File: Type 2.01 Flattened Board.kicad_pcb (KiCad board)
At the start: 4 copper layers, 170 x 170 mm, 68 parts, among them J1 Conn_02x03_Odd_Even, J4 Conn_02x03_Odd_Even, J5 Conn_02x03_Odd_Even, U1 74AHC74, U10 74AHC74, U11 74AHC245, U13 74AHC04, U14 ATmega4809-PF, U16 ATmega4809-PF, U17 74AHC157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

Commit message: Part selection
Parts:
- removed RN2, RN3: R_Network04, Resistor_THT:R_Array_SIP5
- added J2: Conn_01x02, Connector_PinHeader_2.54mm:PinHeader_1x02_P2.54mm_Vertical, F.Cu at (179.7, 107.8)
- added J3: Conn_01x04, Connector_PinHeader_2.54mm:PinHeader_1x04_P2.54mm_Vertical, F.Cu at (175.0, 107.8)
- moved C20 84.1 mm to (108.7, 121.7), turned to -90 degrees
- moved U13 76.4 mm to (114.4, 123.6), turned to 90 degrees
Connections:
- RN1 pad 10: unconnected-(RN1-Pad10) -> /i960/PU2
- RN1 pad 11: unconnected-(RN1-Pad11) -> /i960/PU3
- RN1 pad 12: unconnected-(RN1-Pad12) -> /i960/~{MR_{0}}
- RN1 pad 8: unconnected-(RN1-Pad8) -> /i960/PU0
- RN1 pad 9: unconnected-(RN1-Pad9) -> /i960/PU1
- U13 pad 6: /i960/~{INT3}_OUT -> /i960/i960.~{INT0}
- U13 pad 8: /i960/~{INT0}_OUT -> /i960/i960.~{INT3}
- U14 pad 36: Net-(U13-Pad5) -> /i960/INT3_OUT
- U14 pad 4: Net-(U13-Pad9) -> /i960/INT0_OUT
- U16 pad 10: /i960/EDGE_A -> /i960/EDGE_B
- U16 pad 11: /i960/EDGE_B -> /i960/~{ME_READY}
- U16 pad 9: /i960/~{ME_READY} -> /i960/EDGE_A
- U17 pad 12: /i960/i960.~{INT3} -> Net-(U13-Pad9)
- U17 pad 13: +5V -> GND
- U17 pad 14: /i960/~{INT3}_OUT -> /i960/INT3_OUT
- U17 pad 2: /i960/~{INT0}_OUT -> /i960/INT0_OUT
- U17 pad 3: +5V -> GND
- U17 pad 4: /i960/i960.~{INT0} -> Net-(U13-Pad5)

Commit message: Added feather interrupts as well
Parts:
- removed J1: Conn_02x03_Odd_Even, Connector_IDC:IDC-Header_2x03_P2.54mm_Horizontal
- C20, C5, U13, U17: moved to B.Cu
- U10: value 74AHC74 -> 74AHC174; footprint Package_DIP:DIP-14_W7.62mm_Socket -> Package_SO:SOIC-16_3.9x9.9mm_P1.27mm
- moved J5 171.9 mm to (14.0, 82.2), turned to 180 degrees
- moved J4 119.1 mm to (13.9, 100.7), turned to 180 degrees
- moved C19 106.9 mm to (27.5, 72.8), turned to -90 degrees
- moved U4 99.5 mm to (35.3, 76.9), turned to 90 degrees
- moved U14 86.8 mm to (125.1, 145.0), turned to 90 degrees
- moved U20 85.4 mm to (-78.0, 106.7)
- moved C26 70.3 mm to (136.5, 147.7), turned to 0 degrees
- moved C25 69.7 mm to (146.7, 127.1), turned to 180 degrees
- moved C4 59.0 mm to (87.1, 152.3), turned to 90 degrees
- moved U5 56.2 mm to (54.9, 76.8)
- moved C37 56.2 mm to (62.7, 80.8)
- moved C5 32.0 mm to (136.8, 93.9), turned to 0 degrees
- moved C20 31.8 mm to (125.4, 94.7), turned to 0 degrees
- moved C27 29.4 mm to (167.0, 147.7), turned to 0 degrees
- moved U13 26.4 mm to (127.2, 100.5), turned to 180 degrees
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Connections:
- U10 pad 1: /i960/PU5 -> /i960/~{MR_{0}}
- U10 pad 10: /i960/PU6 -> unconnected-(U10-Pad10)
- U10 pad 11: /i960.CLK -> unconnected-(U10-Pad11)
- U10 pad 12: Net-(U10-Pad12) -> unconnected-(U10-Pad12)
- U10 pad 13: /i960/PU7 -> unconnected-(U10-Pad13)
- U10 pad 14: +5V -> unconnected-(U10-Pad14)
- U10 pad 2: /i960/~{ME_READY} -> unconnected-(U10-Pad2)
- U10 pad 3: /i960.CLK -> unconnected-(U10-Pad3)
- U10 pad 4: /i960/PU4 -> /i960/~{ME_READY}
- U10 pad 5: Net-(U10-Pad12) -> /i960/EDGE_A
- U10 pad 7: GND -> /i960/EDGE_B
- U10 pad 8: unconnected-(U10-Pad8) -> GND
- U10 pad 9: /i960/EDGE_B -> /i960.CLK
- U16 pad 10: /i960/EDGE_B -> /i960/EDGE_A
- U16 pad 9: /i960/EDGE_A -> /i960/EDGE_B

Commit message: Better layout :)
NEed to add a feather breakout as the final part
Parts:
- added XA2: Arduino_Uno_Shield, Arduino_Alarm_Siren:Arduino_Uno_Shield, F.Cu at (115.6, 0.09)
- moved U20 97.2 mm to (6.94, 154.0)
- moved C27 70.1 mm to (97.8, 136.9)
- moved U14 70.1 mm to (55.9, 134.2)
- moved C25 70.1 mm to (77.4, 116.3)
- moved C26 70.1 mm to (67.2, 136.9)
- moved RN1 43.9 mm to (87.1, 145.7), turned to 180 degrees
- moved C30 41.4 mm to (73.8, 85.6)
- moved C31 41.4 mm to (63.7, 106.3)
- moved C32 41.4 mm to (94.2, 106.3)
- moved U16 41.4 mm to (52.3, 103.4)
- moved C4 41.2 mm to (82.3, 111.4)
- moved U10 41.2 mm to (75.9, 109.6)
- moved C1 38.2 mm to (27.6, 90.0)
- moved U1 38.2 mm to (30.4, 97.2)
- moved J2 13.5 mm to (167.9, 101.4), turned to 180 degrees
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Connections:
- U20 pad 2: /UART0.RX -> /UART1.RX
- U20 pad 3: /UART0.TX -> /UART1.TX
- U20 pad 7: /Feather.A5 -> /GCM4.~{FEATHER_INT0}
- U21 pad 2: /GCM4.USART_PIC_TX -> /UART2.RX
- U21 pad 3: /GCM4.USART_PIC_RX -> /UART2.TX
- U21 pad 7: /Feather2.A5 -> /GCM4.~{FEATHER_INT1}
- U3 pad 1: /i960/GCM4.LA0 -> /GCM4.A0
- U3 pad 2: /i960/GCM4.LA1 -> /GCM4.A1
- U3 pad 3: /i960/GCM4.LA2 -> /GCM4.A2
- XA1 pad A10: /GCM4.~{READY} -> /BUS.PB7
- XA1 pad A11: /GCM4.~{CHIPSET_BOOTED} -> /BUS.PB8
- XA1 pad A8: /GCM4.~{INTR0} -> /BUS.PB5
- XA1 pad A9: /GCM4.~{RESET960} -> /BUS.PB6
- XA1 pad D10: /BUS.PB22 -> /GCM4.~{BOOT_SUCCESSFUL}
- XA1 pad D11: /BUS.PB23 -> /GCM4.~{BURST_LAST}
- XA1 pad D2: /BUS.PC18 -> /GCM4.~{READY}
- XA1 pad D26: /BUS.PA12 -> /GCM4.A0
- XA1 pad D27: /BUS.PA13 -> /GCM4.A1
- XA1 pad D28: /BUS.PA14 -> /GCM4.A2
- XA1 pad D3: /BUS.PC19 -> /GCM4.~{CHIPSET_BOOTED}
- XA1 pad D38: /GCM4.HLDA -> /BUS.PB15
- XA1 pad D39: /GCM4.HOLD -> /BUS.PB14
- XA1 pad D4: /BUS.PC20 -> /GCM4.~{RESET960}
- XA1 pad D5: /BUS.PC21 -> /GCM4.~{INTR0}
- XA1 pad D6: /GCM4.A0 -> /GCM4.HOLD
- XA1 pad D7: /GCM4.A1 -> /GCM4.HLDA
- XA1 pad D8: /GCM4.~{BOOT_SUCCESSFUL} -> /GCM4.~{FEATHER_INT1}
- XA1 pad D9: /GCM4.~{BURST_LAST} -> /GCM4.~{FEATHER_INT0}

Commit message: Make sure grouping is right
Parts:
- R4: moved to B.Cu
- moved R4 56.5 mm to (148.2, 96.1), turned to 90 degrees
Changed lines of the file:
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@@
-    )
-  )
-  (footprint "Resistor_SMD:R_0805_2012Metric_Pad1.20x1.40mm_HandSolder" (layer "F.Cu")
-    (at 146.512 39.62448)
-    (descr "Resistor SMD 0805 (2012 Metric), square (rectangular) end terminal, IPC_7351 nominal with elongated pad for handsoldering. (Body size source: IPC-SM-782 page 72, https://www.pcb-3d.com/wordpress/wp-content/uploads/ipc-sm-782a_amendment_1_and_2.pdf), generated with kicad-footprint-generator")
-    (tags "resistor handsolder")
-    (property "Sheetfile" "i960.kicad_sch")
-    (property "Sheetname" "i960")
-    (attr smd)
-    (fp_text reference "R4" (at 0 -1.65) (layer "F.SilkS")
-      (effects (font (size 1 1) (thickness 0.15)))
-    )
-    (fp_text value "10k" (at 0 1.65) (layer "F.Fab")
-      (effects (font (size 1 1) (thickness 0.15)))
-    )
-    (fp_text user "${REFERENCE}" (at 0 0) (layer "F.Fab")
-      (effects (font (size 0.5 0.5) (thickness 0.08)))
-    )
-    (fp_line (start -0.227064 -0.735) (end 0.227064 -0.735) (layer "F.SilkS") (width 0.12))
-    (fp_line (start -0.227064 0.735) (end 0.227064 0.735) (layer "F.SilkS") (width 0.12))
-    (fp_line (start -1.85 0.95) (end -1.85 -0.95) (layer "F.CrtYd") (width 0.05))
-    (fp_line (start -1.85 -0.95) (end 1.85 -0.95) (layer "F.CrtYd") (width 0.05))
-    (fp_line (start 1.85 -0.95) (end 1.85 0.95) (layer "F.CrtYd") (width 0.05))
-    (fp_line (start 1.85 0.95) (end -1.85 0.95) (layer "F.CrtYd") (width 0.05))
-    (fp_line (start -1 -0.625) (end 1 -0.625) (layer "F.Fab") (width 0.1))
-    (fp_line (start -1 0.625) (end -1 -0.625) (layer "F.Fab") (width 0.1))
-    (fp_line (start 1 -0.625) (end 1 0.625) (layer "F.Fab") (width 0.1))
-    (fp_line (start 1 0.625) (end -1 0.625) (layer "F.Fab") (width 0.1))
-    (pad "1" smd roundrect (at -1 0) (size 1.2 1.4) (layers "F.Cu" "F.Paste" "F.Mask") (roundrect_rratio 0.208333)
-      (net 2 "+5V") (pintype "passive"))
-    (pad "2" smd roundrect (at 1 0) (size 1.2 1.4) (layers "F.Cu" "F.Paste" "F.Mask") (roundrect_rratio 0.208333)
-      (net 142 "/i960/~{BUF_ENABLE}") (pintype "passive"))
-    (model "${KICAD6_3DMODEL_DIR}/Resistor_SMD.3dshapes/R_0805_2012Metric.wrl"
-      (offset (xyz 0 0 0))
-      (scale (xyz 1 1 1))
-      (rotate (xyz 0 0 0))
     )
   )
@@
     )
   )
+  (footprint "Resistor_SMD:R_0805_2012Metric_Pad1.20x1.40mm_HandSolder" (layer "B.Cu")
+    (at 148.22932 96.06026 90)
+    (descr "Resistor SMD 0805 (2012 Metric), square (rectangular) end terminal, IPC_7351 nominal with elongated pad for handsoldering. (Body size source: IPC-SM-782 page 72, https://www.pcb-3d.com/wordpress/wp-content/uploads/ipc-sm-782a_amendment_1_and_2.pdf), generated with kicad-footprint-generator")
+    (tags "resistor handsolder")
+    (property "Sheetfile" "i960.kicad_sch")
+    (property "Sheetname" "i960")
+    (attr smd)
+    (fp_text reference "R4" (at 2.5781 -0.07112 180) (layer "B.SilkS")
+      (effects (font (size 1 1) (thickness 0.15)) (justify mirror))
+    )
+    (fp_text value "10k" (at 0 -1.65 90) (layer "B.Fab")
+      (effects (font (size 1 1) (thickness 0.15)) (justify mirror))
+    )
+    (fp_text user "${REFERENCE}" (at 0 0 90) (layer "B.Fab")
+      (effects (font (size 0.5 0.5) (thickness 0.08)) (justify mirror))
+    )
+    (fp_line (start -0.227064 0.735) (end 0.227064 0.735) (layer "B.SilkS") (width 0.12))
+    (fp_line (start -0.227064 -0.735) (end 0.227064 -0.735) (layer "B.SilkS") (width 0.12))
+    (fp_line (start -1.85 -0.95) (end -1.85 0.95) (layer "B.CrtYd") (width 0.05))
+    (fp_line (start -1.85 0.95) (end 1.85 0.95) (layer "B.CrtYd") (width 0.05))
+    (fp_line (start 1.85 0.95) (end 1.85 -0.95) (layer "B.CrtYd") (width 0.05))
+    (fp_line (start 1.85 -0.95) (end -1.85 -0.95) (layer "B.CrtYd") (width 0.05))
+    (fp_line (start -1 0.625) (end 1 0.625) (layer "B.Fab") (width 0.1))
+    (fp_line (start -1 -0.625) (end -1 0.625) (layer "B.Fab") (width 0.1))
+    (fp_line (start 1 0.625) (end 1 -0.625) (layer "B.Fab") (width 0.1))
+    (fp_line (start 1 -0.625) (end -1 -0.625) (layer "B.Fab") (width 0.1))
+    (pad "1" smd roundrect (at -1 0 90) (size 1.2 1.4) (layers "B.Cu" "B.Paste" "B.Mask") (roundrect_rratio 0.208333)
+      (net 2 "+5V") (pintype "passive"))
+    (pad "2" smd roundrect (at 1 0 90) (size 1.2 1.4) (layers "B.Cu" "B.Paste" "B.Mask") (roundrect_rratio 0.208333)
+      (net 142 "/i960/~{BUF_ENABLE}") (pintype "passive"))
+    (model "${KICAD6_3DMODEL_DIR}/Resistor_SMD.3dshapes/R_0805_2012Metric.wrl"
+      (offset (xyz 0 0 0))
+      (scale (xyz 1 1 1))
+      (rotate (xyz 0 0 0))
+    )
+  )
   (footprint "Capacitor_SMD:C_0805_2012Metric_Pad1.18x1.45mm_HandSolder" (layer "B.Cu")
     (at 139.35202 82.9183 180)
@@
     )
   )
+  (group "" (id 6c7201de-2da6-4004-b4bc-da86477287fa)
+    (members
+      62ee2ea2-7b33-4135-a0d7-c5f20877dd93
+      9ebd9c07-eb9a-4788-9581-0ba662c943a1
+    )
+  )

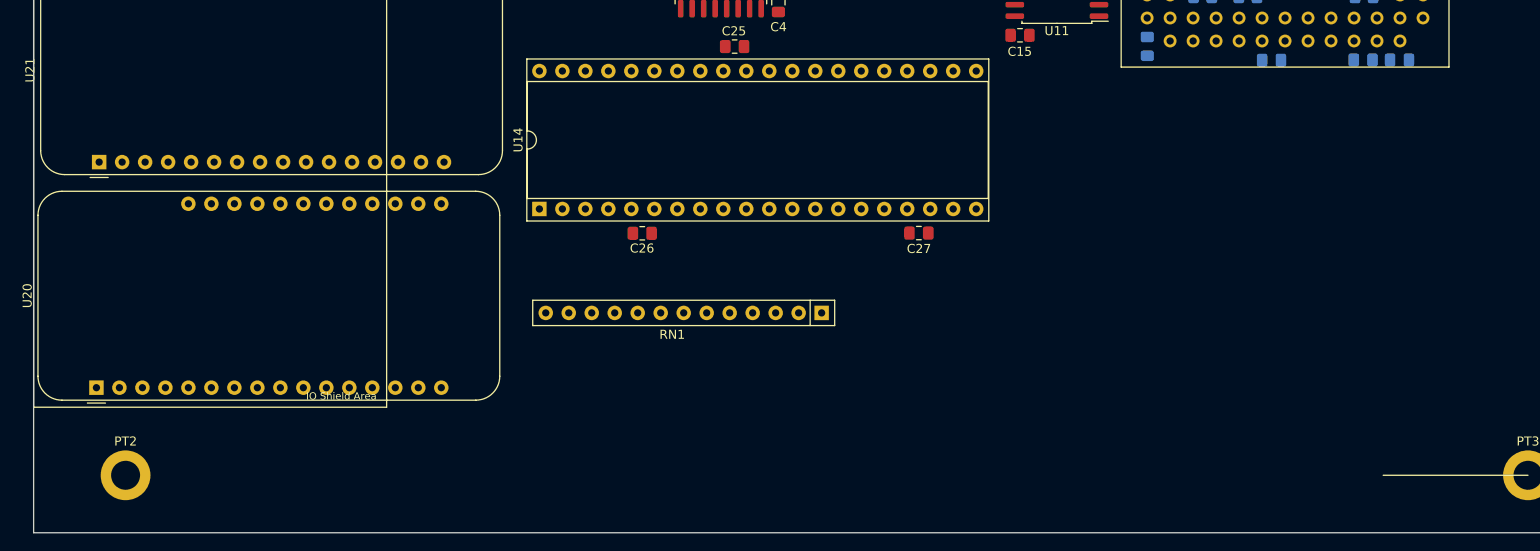
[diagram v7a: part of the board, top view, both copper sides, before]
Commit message: Added a new 9 pin breakout header for me pins
PORTA on the ME is now free. CLK is now connected to PD7. That way I can
reuse all of PORTA for whatever I want in the future.
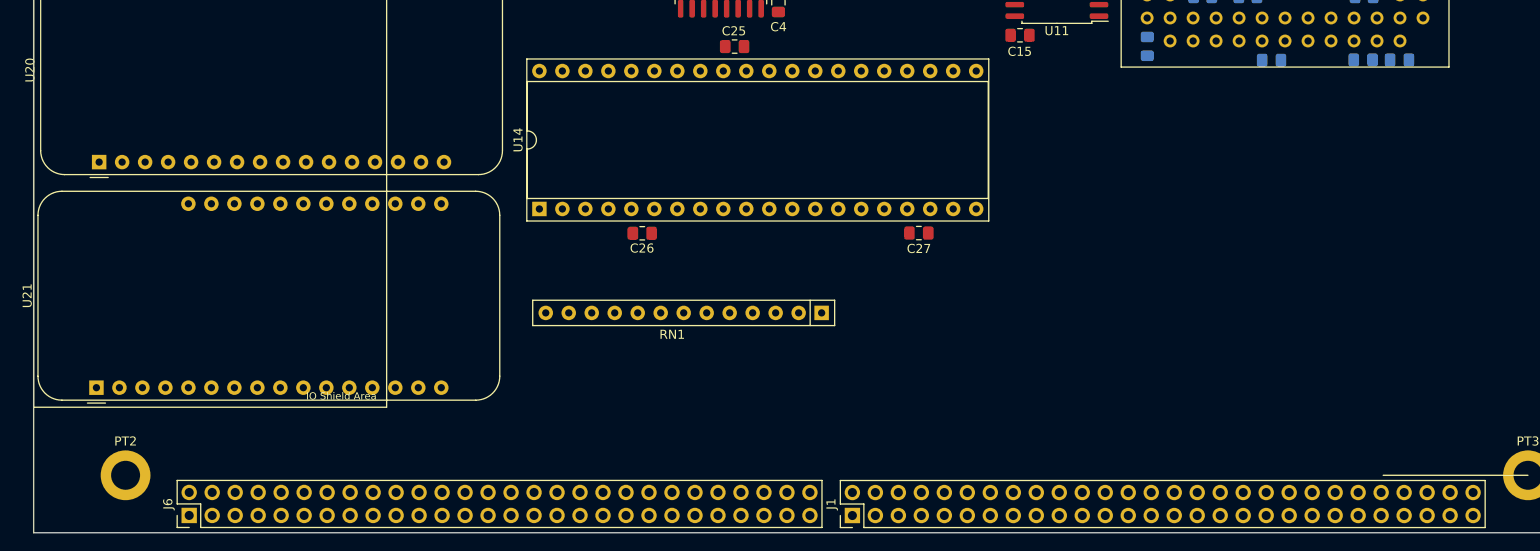
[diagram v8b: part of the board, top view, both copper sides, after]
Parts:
- added J1: Conn_02x28_Odd_Even, Connector_PinHeader_2.54mm:PinHeader_2x28_P2.54mm_Vertical, F.Cu at (90.5, 168.1)
- added J6: Conn_02x28_Odd_Even, Connector_PinHeader_2.54mm:PinHeader_2x28_P2.54mm_Vertical, F.Cu at (17.2, 168.1)
- renumbered U21 to U20, U20 to U21
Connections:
- U20 pad 1: /Feather2.FREE -> /Feather.FREE
- U20 pad 10: /Feather2.A2 -> /Feather.A2
- U20 pad 11: /Feather2.A1 -> /Feather.A1
- U20 pad 12: /Feather2.A0 -> /Feather.A0
- U20 pad 14: /Feather2.AREF -> /Feather.AREF
- U20 pad 18: /Feather2.EN -> /Feather.EN
- U20 pad 2: /UART2.RX -> /UART1.RX
- U20 pad 20: /Feather2.D13 -> /Feather.D13
- U20 pad 21: /Feather2.D12 -> /Feather.D12
- U20 pad 22: /Feather2.D11 -> /Feather.D11
- U20 pad 23: /Feather2.D10 -> /Feather.D10
- U20 pad 24: /Feather2.D9 -> /Feather.D9
- U20 pad 25: /Feather2.D6 -> /Feather.D6
- U20 pad 26: /Feather2.D5 -> /Feather.D5
- U20 pad 27: /Feather2.SCL -> /Feather.SCL
- U20 pad 28: /Feather2.SDA -> /Feather.SDA
- U20 pad 3: /UART2.TX -> /UART1.TX
- U20 pad 4: /Feather2.MISO -> /Feather.MISO
- U20 pad 5: /Feather2.MOSI -> /Feather.MOSI
- U20 pad 6: /Feather2.SCK -> /Feather.SCK
- U20 pad 7: /GCM4.~{FEATHER_INT1} -> /GCM4.~{FEATHER_INT0}
- U20 pad 8: /Feather2.A4 -> /Feather.A4
- U20 pad 9: /Feather2.A3 -> /Feather.A3
- U21 pad 1: /Feather.FREE -> /Feather2.FREE
- U21 pad 10: /Feather.A2 -> /Feather2.A2
- U21 pad 11: /Feather.A1 -> /Feather2.A1
- U21 pad 12: /Feather.A0 -> /Feather2.A0
- U21 pad 14: /Feather.AREF -> /Feather2.AREF
- U21 pad 18: /Feather.EN -> /Feather2.EN
- U21 pad 2: /UART1.RX -> /UART2.RX
- U21 pad 20: /Feather.D13 -> /Feather2.D13
- U21 pad 21: /Feather.D12 -> /Feather2.D12
- U21 pad 22: /Feather.D11 -> /Feather2.D11
- U21 pad 23: /Feather.D10 -> /Feather2.D10
- U21 pad 24: /Feather.D9 -> /Feather2.D9
- U21 pad 25: /Feather.D6 -> /Feather2.D6
- U21 pad 26: /Feather.D5 -> /Feather2.D5
- U21 pad 27: /Feather.SCL -> /Feather2.SCL
- U21 pad 28: /Feather.SDA -> /Feather2.SDA
- U21 pad 3: /UART1.TX -> /UART2.TX
- U21 pad 4: /Feather.MISO -> /Feather2.MISO
- U21 pad 5: /Feather.MOSI -> /Feather2.MOSI
- U21 pad 6: /Feather.SCK -> /Feather2.SCK
- U21 pad 7: /GCM4.~{FEATHER_INT0} -> /GCM4.~{FEATHER_INT1}
- U21 pad 8: /Feather.A4 -> /Feather2.A4
- U21 pad 9: /Feather.A3 -> /Feather2.A3
